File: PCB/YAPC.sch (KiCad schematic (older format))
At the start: 0 parts

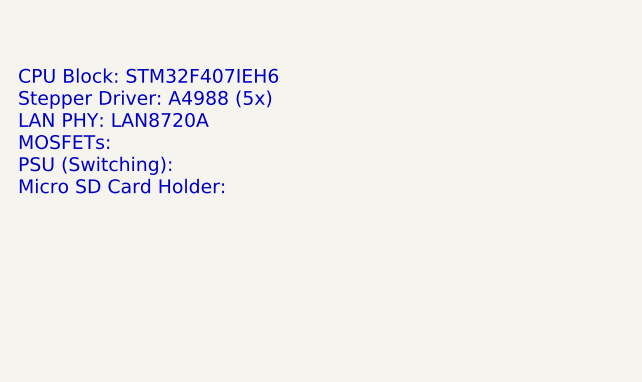
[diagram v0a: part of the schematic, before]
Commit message: Start applying power and config to the CPU
Start with the cpu power scheme and some of the external configuration
needed.
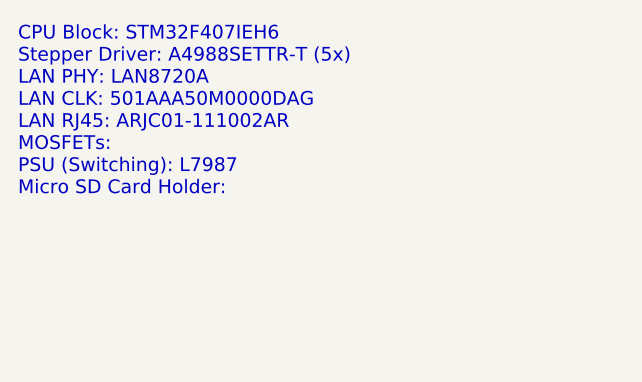
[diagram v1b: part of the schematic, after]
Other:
- note added: "CPU Block: STM32F407IEH6\nStepper Driver: A4988SETTR-T (5x)\nLAN PHY: LAN8720A\nLAN CLK: 501AAA50M0000DAG\nLAN RJ45: ARJC01-111002AR\nMOSFETs:\nPSU (Switching): L7987\nMicro SD Card Holder:"
- note removed: "CPU Block: STM32F407IEH6\nStepper Driver: A4988 (5x)\nLAN PHY: LAN8720A\nMOSFETs:\nPSU (Switching):\nMicro SD Card Holder:"
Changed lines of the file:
@@
 $EndDescr
 Text Notes 5050 3600 0    60   ~ 0
-CPU Block: STM32F407IEH6\nStepper Driver: A4988 (5x)\nLAN PHY: LAN8720A\nMOSFETs:\nPSU (Switching):\nMicro SD Card Holder:
+CPU Block: STM32F407IEH6\nStepper Driver: A4988SETTR-T (5x)\nLAN PHY: LAN8720A\nLAN CLK: 501AAA50M0000DAG\nLAN RJ45: ARJC01-111002AR\nMOSFETs:\nPSU (Switching): L7987\nMicro SD Card Holder:
 $Sheet
 S 9400 5900 2250 1650
